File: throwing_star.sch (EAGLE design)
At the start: 6 parts

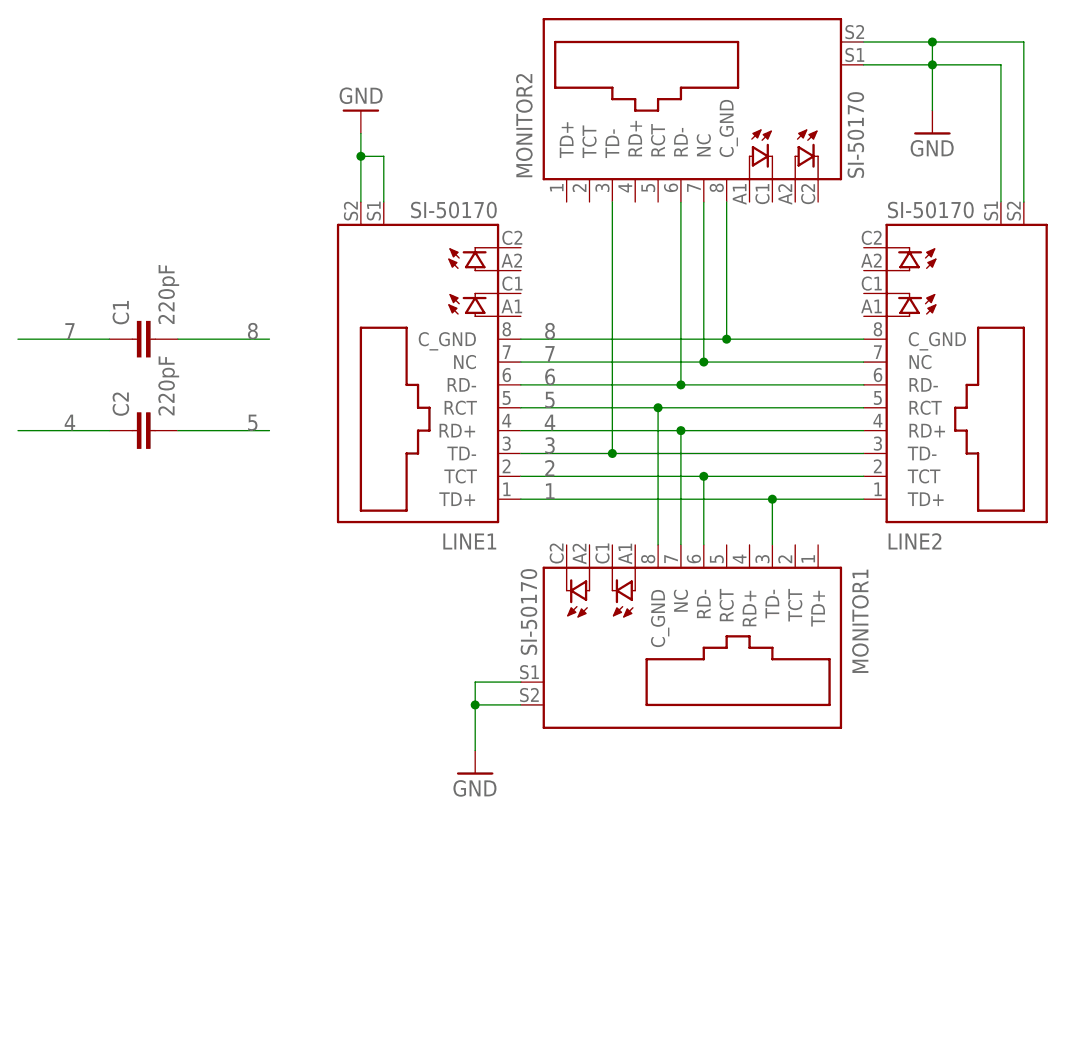
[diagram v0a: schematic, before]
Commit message: change rj45 jacks and reroute
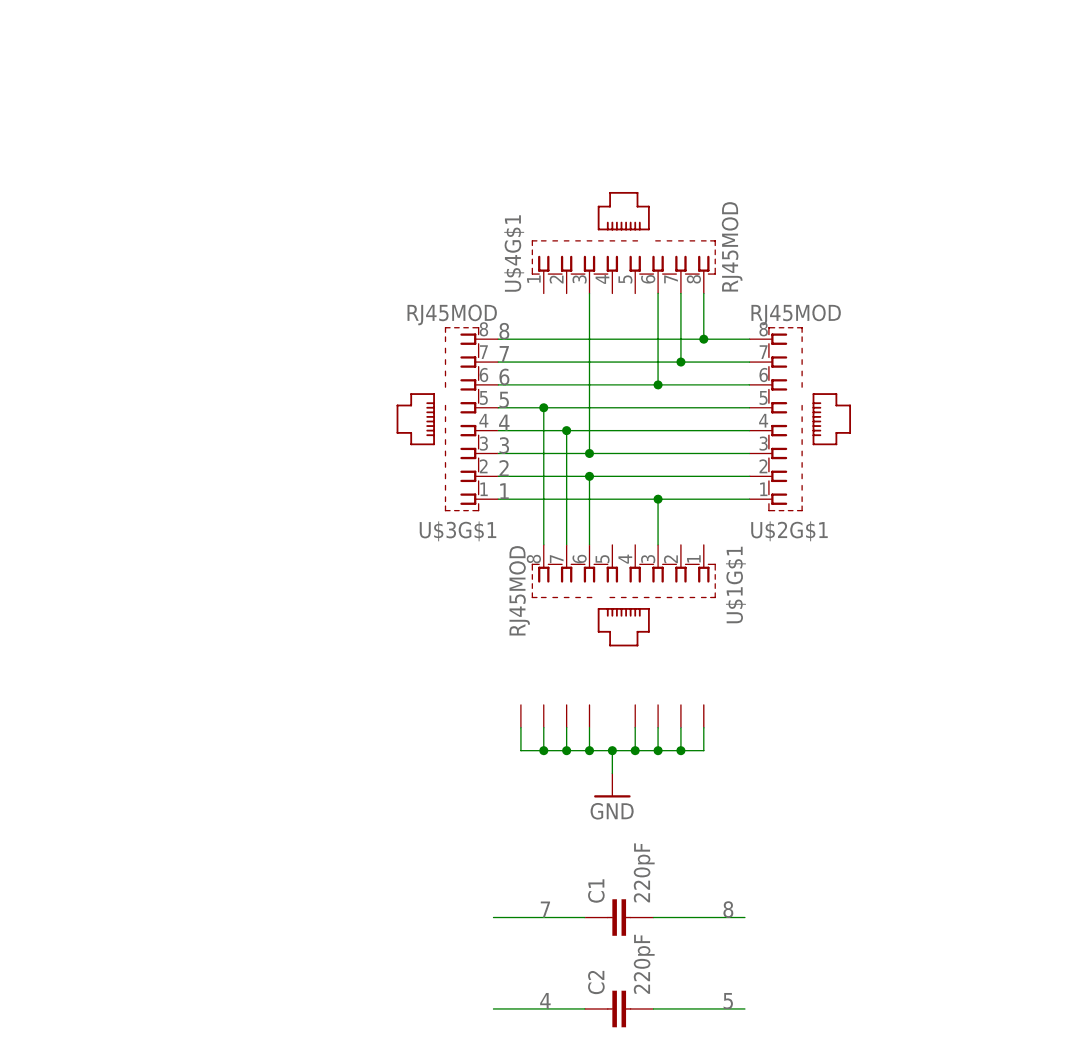
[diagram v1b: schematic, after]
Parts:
- removed LINE1, LINE2, MONITOR1, MONITOR2: SI-50170, con-stewart:SI-50170
- added U$1, U$2, U$3, U$4: RJ45MOD, con-appsys:RJ45MOD
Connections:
- net 1: now also U$1G$1.3, U$2G$1.1, U$3G$1.1; no longer LINE1.TD+, LINE2.TD+, MONITOR1.TD-
- net 2: now also U$1G$1.6, U$2G$1.2, U$3G$1.2; no longer LINE1.TCT, LINE2.TCT, MONITOR1.RD-
- net 3: now also U$2G$1.3, U$3G$1.3, U$4G$1.3; no longer LINE1.TD-, LINE2.TD-, MONITOR2.TD-
- net 4: now also U$1G$1.7, U$2G$1.4, U$3G$1.4; no longer LINE1.RD+, LINE2.RD+, MONITOR1.NC
- net 5: now also U$1G$1.8, U$2G$1.5, U$3G$1.5; no longer LINE1.RCT, LINE2.RCT, MONITOR1.C_GND
- net 6: now also U$2G$1.6, U$3G$1.6, U$4G$1.6; no longer LINE1.RD-, LINE2.RD-, MONITOR2.RD-
- net 7: now also U$2G$1.7, U$3G$1.7, U$4G$1.7; no longer LINE1.NC, LINE2.NC, MONITOR2.NC
- net 8: now also U$2G$1.8, U$3G$1.8, U$4G$1.8; no longer LINE1.C_GND, LINE2.C_GND, MONITOR2.C_GND
- net GND: now also U$1G$2.1, U$1G$3.1, U$2G$2.1, U$2G$3.1, U$3G$2.1, U$3G$3.1, U$4G$2.1, U$4G$3.1; no longer LINE1.S1, LINE1.S2, LINE2.S1, LINE2.S2, MONITOR1.S1, MONITOR1.S2, MONITOR2.S1, MONITOR2.S2
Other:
- moved on the sheet: C1, C2
